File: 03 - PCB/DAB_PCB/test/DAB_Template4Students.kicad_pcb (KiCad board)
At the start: 2 copper layers, 240 x 200 mm, 32 parts

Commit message: lined almost every footprint
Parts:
- added C25: 1000pF, Capacitor_SMD:C_1206_3216Metric, F.Cu at (221.6, 79.1)
- added C5: 1000pF, Capacitor_SMD:C_1206_3216Metric, F.Cu at (221.6, 75.7)
- added C_boot1: 100nF, Capacitor_SMD:C_1206_3216Metric, F.Cu at (129.7, 124.8)
- added C_boot2: 100nF, Capacitor_SMD:C_1206_3216Metric, F.Cu at (129.7, 128.1)
- added C_boot3: 0.22µF, Capacitor_SMD:C_1206_3216Metric, F.Cu at (136.7, 137.2)
- added C_boot4: 0.22µF, Capacitor_SMD:C_1206_3216Metric, F.Cu at (136.7, 140.5)
- added C_fil1: 2.2µF, Capacitor_SMD:C_1206_3216Metric, F.Cu at (221.6, 82.4)
- added C_fil2: 2.2µF, Capacitor_SMD:C_1206_3216Metric, F.Cu at (221.6, 85.8)
- added C_fil3: 2.2µF, Capacitor_SMD:C_1206_3216Metric, F.Cu at (221.6, 89.1)
- added C_vdd1: 2.2µF, Capacitor_SMD:C_1206_3216Metric, F.Cu at (129.7, 131.5)
- added C_vdd2: 2.2µF, Capacitor_SMD:C_1206_3216Metric, F.Cu at (129.7, 134.8)
- added C_vdd3: 4.7µF, Capacitor_SMD:C_1206_3216Metric, F.Cu at (136.7, 143.9)
- added C_vdd4: 4.7µF, Capacitor_SMD:C_1206_3216Metric, F.Cu at (136.7, 147.2)
- added C_vdd5: 10nF, Capacitor_SMD:C_1206_3216Metric, F.Cu at (221.6, 92.5)
- added C_vdd6: 10nF, Capacitor_SMD:C_1206_3216Metric, F.Cu at (221.6, 95.8)
- added Chi1: 22pF, Capacitor_SMD:C_1206_3216Metric, F.Cu at (142.4, 137.2)
- added Chi2: 22pF, Capacitor_SMD:C_1206_3216Metric, F.Cu at (142.4, 140.5)
- added Chi3: 22pF, Capacitor_SMD:C_1206_3216Metric, F.Cu at (142.4, 143.9)
- added Chi4: 22pF, Capacitor_SMD:C_1206_3216Metric, F.Cu at (142.4, 147.2)
- added Cli1: 22pF, Capacitor_SMD:C_1206_3216Metric, F.Cu at (148.0, 137.2)
- added Cli2: 22pF, Capacitor_SMD:C_1206_3216Metric, F.Cu at (148.0, 140.5)
- added Cli3: 22pF, Capacitor_SMD:C_1206_3216Metric, F.Cu at (148.0, 143.9)
- added Cli4: 22pF, Capacitor_SMD:C_1206_3216Metric, F.Cu at (148.0, 147.2)
- added D1: LMB14S-TP, DAB:LMB14STP, F.Cu at (197.9, 163.0)
- added IC1: UCC27288DR, DAB:SOIC127P600X175-8N, F.Cu at (122.7, 119.8)
- added IC2: UCC27288DR, DAB:SOIC127P600X175-8N, F.Cu at (122.6, 126.4)
- added IC3: UCC27288DR, DAB:SOIC127P600X175-8N, F.Cu at (122.6, 132.9)
- added IC4: UCC27288DR, DAB:SOIC127P600X175-8N, F.Cu at (122.6, 139.5)
- added IC5: INA201AID, DAB:SOIC127P600X175-8N, F.Cu at (206.3, 77.3)
- added IC6: INA201AID, DAB:SOIC127P600X175-8N, F.Cu at (206.3, 83.9)
- added IC7: INA201AID, DAB:SOIC127P600X175-8N, F.Cu at (206.3, 90.4)
- added IC8: INA201AID, DAB:SOIC127P600X175-8N, F.Cu at (206.3, 97.0)
- added LED1: WP710A10LGD, DAB:WP710A10LID, F.Cu at (171.8, 160.1)
- added LED2: WP710A10LGD, DAB:WP710A10LID, F.Cu at (178.1, 160.1)
- added LED3: WP710A10LGD, DAB:WP710A10LID, F.Cu at (184.4, 160.1)
- added LED4: WP710A10LGD, DAB:WP710A10LID, F.Cu at (190.7, 160.1)
- added LED4: WP710A10LGD, DAB:WP710A10LID, F.Cu at (227.6, 76.3)
- added LED6: WP710A10LID, DAB:WP710A10LID, F.Cu at (171.8, 167.1)
- added LED7: WP710A10LGD, DAB:WP710A10LID, F.Cu at (178.1, 167.1)
- added LED8: WP710A10LGD, DAB:WP710A10LID, F.Cu at (184.4, 167.1)
- added R17: 200k, Resistor_SMD:R_1206_3216Metric, F.Cu at (204.8, 59.2)
- added R18: 50, Resistor_SMD:R_1206_3216Metric, F.Cu at (204.8, 62.5)
- added R19: 50, Resistor_SMD:R_1206_3216Metric, F.Cu at (204.8, 65.8)
- added Rdiv1: 23.2k, Resistor_SMD:R_1206_3216Metric, F.Cu at (204.8, 69.1)
- added Rdiv2: 10k, Resistor_SMD:R_1206_3216Metric, F.Cu at (204.8, 72.4)
- added Rdiv3: 23.2k, Resistor_SMD:R_1206_3216Metric, F.Cu at (210.4, 59.2)
- added Rdiv4: 10k, Resistor_SMD:R_1206_3216Metric, F.Cu at (210.4, 62.5)
- added Rfil1: 10, Resistor_SMD:R_1206_3216Metric, F.Cu at (210.4, 65.8)
- added Rfil2: 10, Resistor_SMD:R_1206_3216Metric, F.Cu at (210.4, 69.1)
- added Rfil5: 10, Resistor_SMD:R_1206_3216Metric, F.Cu at (210.4, 72.4)
- added Rfil6: 10, Resistor_SMD:R_1206_3216Metric, F.Cu at (216.0, 59.2)
- added Rfil8: 10, Resistor_SMD:R_1206_3216Metric, F.Cu at (216.0, 62.5)
- added Rfil9: 10, Resistor_SMD:R_1206_3216Metric, F.Cu at (216.0, 65.8)
- added Rg1: 10, Resistor_SMD:R_1206_3216Metric, F.Cu at (136.7, 117.3)
- added Rg2: 10, Resistor_SMD:R_1206_3216Metric, F.Cu at (136.7, 120.6)
- added Rg3: 10, Resistor_SMD:R_1206_3216Metric, F.Cu at (136.7, 123.9)
- added Rg4: 10, Resistor_SMD:R_1206_3216Metric, F.Cu at (136.7, 127.2)
- added Rg5: 10, Resistor_SMD:R_1206_3216Metric, F.Cu at (136.7, 130.5)
- added Rg6: 10, Resistor_SMD:R_1206_3216Metric, F.Cu at (136.7, 133.8)
- added Rg7: 10, Resistor_SMD:R_1206_3216Metric, F.Cu at (142.3, 117.3)
- added Rg8: 10, Resistor_SMD:R_1206_3216Metric, F.Cu at (142.3, 120.6)
- added Rgs1: 10k, Resistor_SMD:R_1206_3216Metric, F.Cu at (142.3, 123.9)
- added Rgs2: 10k, Resistor_SMD:R_1206_3216Metric, F.Cu at (142.3, 127.2)
- added Rgs3: 10k, Resistor_SMD:R_1206_3216Metric, F.Cu at (142.3, 130.5)
- added Rgs4: 10k, Resistor_SMD:R_1206_3216Metric, F.Cu at (142.3, 133.8)
- added Rgs5: 10k, Resistor_SMD:R_1206_3216Metric, F.Cu at (147.9, 117.3)
- added Rgs6: 10k, Resistor_SMD:R_1206_3216Metric, F.Cu at (147.9, 120.6)
- added Rgs7: 10k, Resistor_SMD:R_1206_3216Metric, F.Cu at (147.9, 123.9)
- added Rgs8: 10k, Resistor_SMD:R_1206_3216Metric, F.Cu at (147.9, 127.2)
- added Rhi1: 2.2k, Resistor_SMD:R_1206_3216Metric, F.Cu at (147.9, 130.5)
- added Rhi2: 2.2k, Resistor_SMD:R_1206_3216Metric, F.Cu at (147.9, 133.8)
- added Rhi3: 2.2k, Resistor_SMD:R_1206_3216Metric, F.Cu at (153.5, 117.3)
- added Rhi4: 2.2k, Resistor_SMD:R_1206_3216Metric, F.Cu at (153.5, 120.6)
- added Rli1: 2.2k, Resistor_SMD:R_1206_3216Metric, F.Cu at (153.5, 123.9)
- added Rli2: 2.2k, Resistor_SMD:R_1206_3216Metric, F.Cu at (153.5, 127.2)
- added Rli3: 2.2k, Resistor_SMD:R_1206_3216Metric, F.Cu at (153.5, 130.5)
- added Rli4: 2.2k, Resistor_SMD:R_1206_3216Metric, F.Cu at (153.5, 133.8)
- added RrtE1: Variable Resistor, DAB:TRIMMER CT-6EP, F.Cu at (214.6, 78.2)
- added RrtE2: 10k, DAB:TRIMMER CT-6EP, F.Cu at (214.6, 86.4)
- added RrtE3: 10k, DAB:TRIMMER CT-6EP, F.Cu at (214.6, 94.7)
- added Shunt1: 25m, Resistor_SMD:R_2512_6332Metric, F.Cu at (223.2, 60.0)
- added Shunt2: 10m, Resistor_SMD:R_2512_6332Metric, F.Cu at (223.2, 64.9)
- added Shunt3: 10m, Resistor_SMD:R_2512_6332Metric, F.Cu at (223.2, 69.8)
- added Tr1: Transformer, DAB:B66362X1014T001, F.Cu at (207.2, 122.1)
- moved C? 220.5 mm to (119.5, 33.0)
- moved D? 220.5 mm to (110.0, 95.0)
- moved J? 220.5 mm to (69.6, 70.5)
- moved LED? 220.5 mm to (158.6, 31.9)
- moved Me? 220.5 mm to (59.8, 32.0)
- moved Me? 220.5 mm to (65.8, 32.0)
- moved R? 220.5 mm to (62.3, 94.2)
- moved R? 220.5 mm to (99.8, 33.0)
- moved SWH?? 220.5 mm to (145.8, 35.6)
- moved C? 220.5 mm to (110.8, 33.0)
- moved C? 220.5 mm to (115.2, 33.0)
- moved D? 220.5 mm to (148.8, 96.0)
- moved HS? 220.5 mm to (129.0, 78.5)
- moved IC? 220.5 mm to (85.6, 95.0)
- moved IC? 220.5 mm to (102.7, 94.1)
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
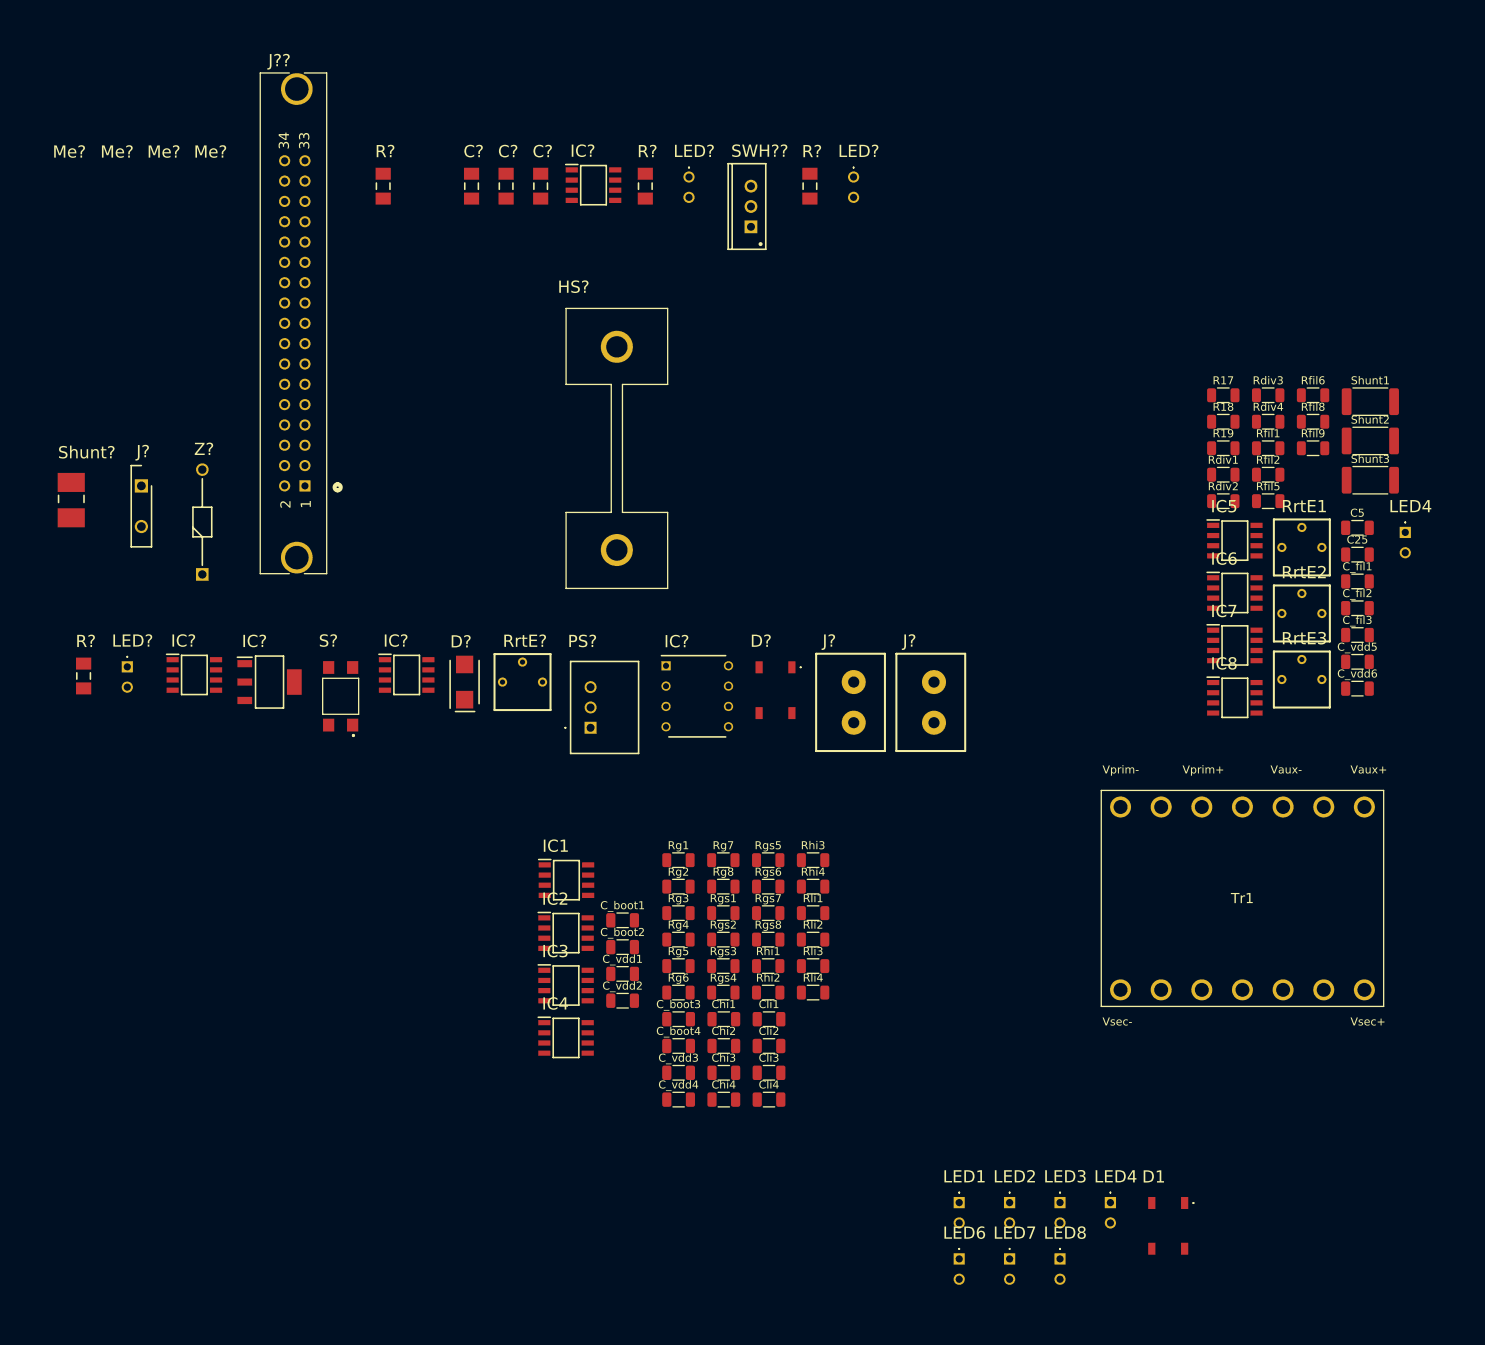
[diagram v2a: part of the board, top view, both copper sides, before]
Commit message: added testpoints
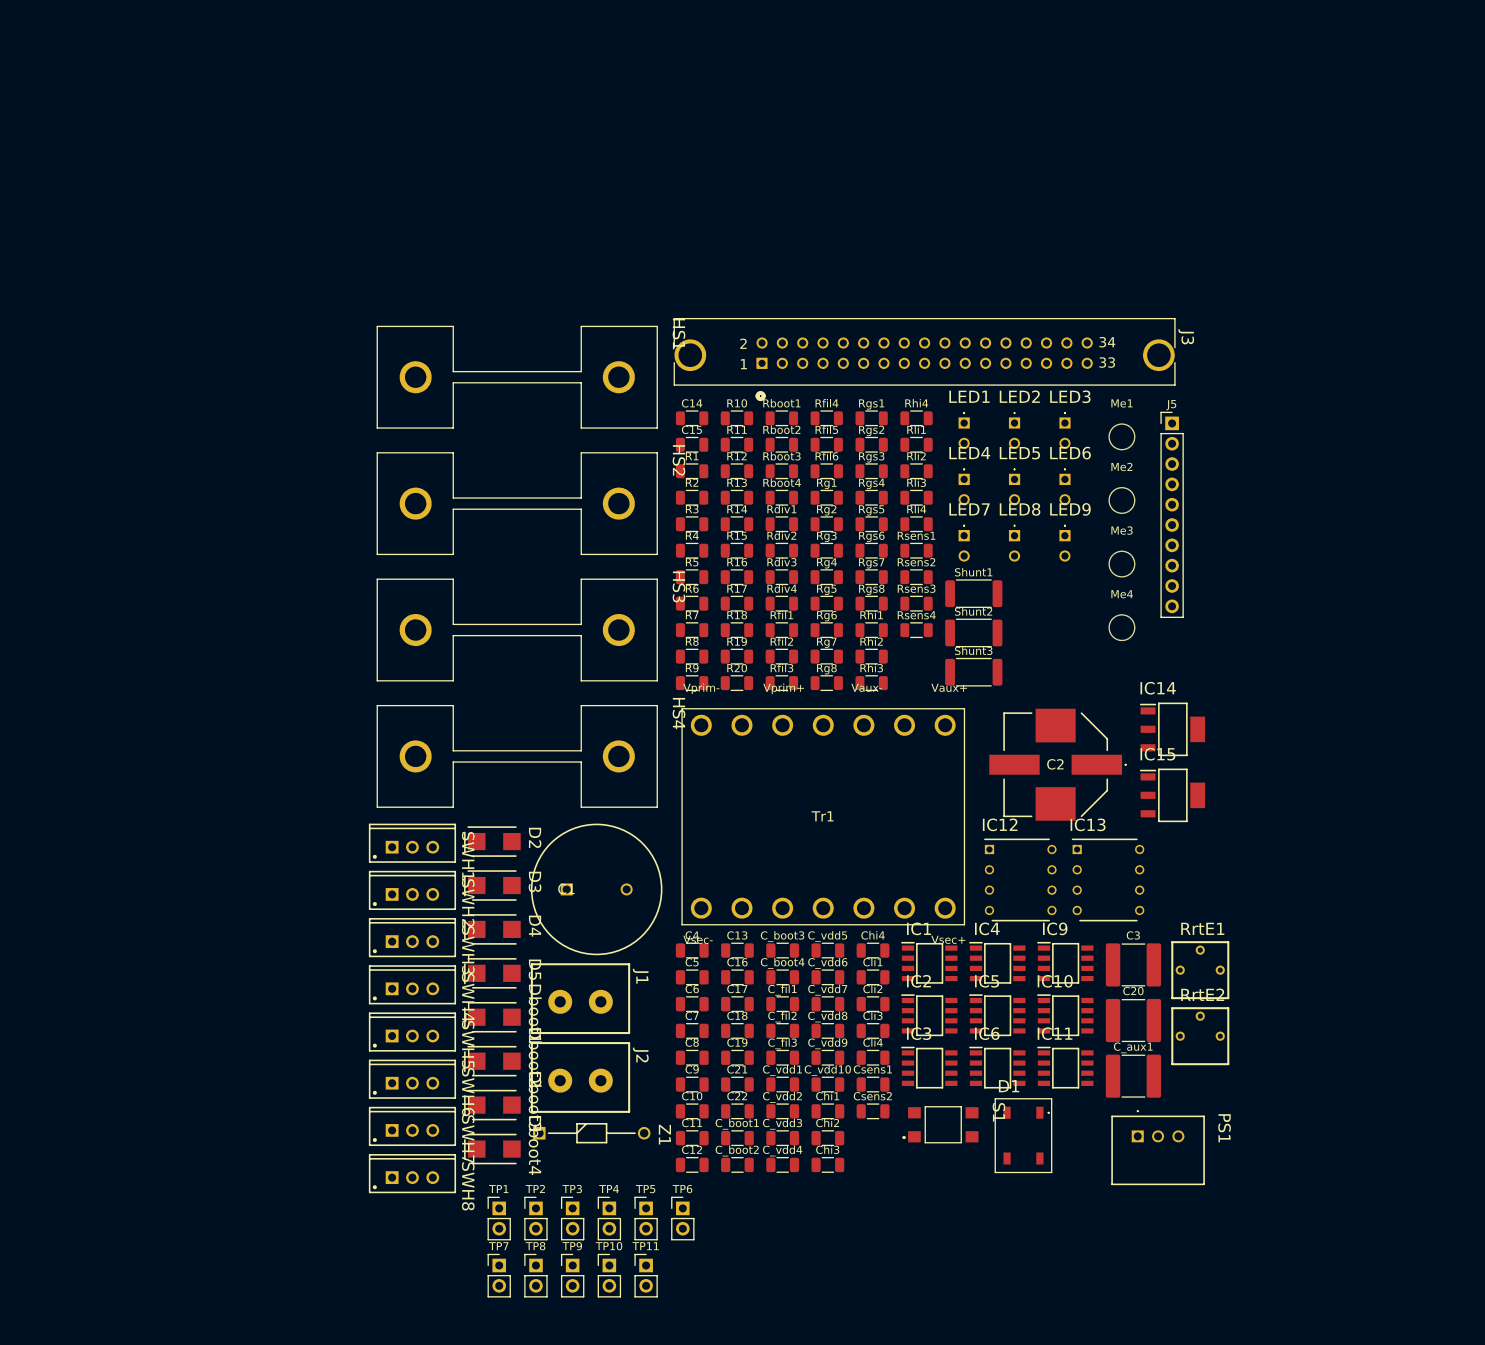
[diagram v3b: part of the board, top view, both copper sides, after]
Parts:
- removed C25: 1000pF, Capacitor_SMD:C_1206_3216Metric
- removed C? (x2): 1uF, DAB_EE365:1206
- removed C?: Put Value Here!, DAB_EE365:1206
- removed D?: LMB14S-TP, DAB_EE365:LMB14STP
- removed D?: ES2C, DAB_EE365:DIOM5436X244N
- removed HS?: Heatsink, DAB_EE365:Heatsink EA-T220
- removed IC7, IC8: INA201AID, DAB:SOIC127P600X175-8N
- removed IC?: AZ1117IH-3.3TRG1, DAB_EE365:SOT230P700X180-4N
- removed IC?: INA201AID, DAB_EE365:SOIC127P600X175-8N
- removed IC?: MCP6241-E_P, DAB_EE365:DIP781W56P254L950H533Q8N
- removed IC?: UCC27288DR, DAB_EE365:SOIC127P600X175-8N
- removed IC?: UA78L12ACDR, DAB_EE365:SOIC127P600X175-8N
- removed J?: test point, DAB_EE365:test point
- removed J? (x2): , DAB_EE365:PHOENIX 1755736
- removed J??: N3431-6302RB, DAB_EE365:3M_N3431-6302RB
- removed the LED4 at (190.7, 160.1)
- removed the LED4 at (227.6, 76.3)
- removed LED? (x2): WP710A10LGD, DAB_EE365:WP710A10LGD
- removed LED?: WP710A10LID, DAB_EE365:WP710A10LID
- removed Me? (x4): M3-Hole, DAB_EE365:M3
- removed PS?: 173951275, DAB_EE365:173951275
- removed R? (x4): Put Value here!, DAB_EE365:1206
- removed Rfil8, Rfil9: 10, Resistor_SMD:R_1206_3216Metric
- removed RrtE3: 10k, DAB:TRIMMER CT-6EP
- removed RrtE?: Variable Resistor, DAB_EE365:TRIMMER CT-6EP
- removed S?: TL3305BF100QG, DAB_EE365:TL3305BF160QG
- removed SWH??: Put MOSFET Part Number Here!, PCB1:TO-220AB
- removed Shunt?: Put Value Here!, DAB_PCB:CSNL2512FT5L00
- removed Z?: 1N4750A-TR, SamacSys:DIOAD1310W86L370D235
- added C1: 680µF, DAB:CAPPRD750W80D1625H3750, F.Cu at (122.7, 120.9)
- added C10: 10µF, Capacitor_SMD:C_1206_3216Metric, F.Cu at (138.4, 148.7)
- added C11: 10µF, Capacitor_SMD:C_1206_3216Metric, F.Cu at (138.4, 152.0)
- added C12: 10µF, Capacitor_SMD:C_1206_3216Metric, F.Cu at (138.4, 155.4)
- added C13: 10µF, Capacitor_SMD:C_1206_3216Metric, F.Cu at (144.1, 128.6)
- added C14: 1uF, Resistor_SMD:R_1206_3216Metric, F.Cu at (138.4, 62.0)
- added C15: 1uF, Resistor_SMD:R_1206_3216Metric, F.Cu at (138.4, 65.3)
- added C16: 1000pF, Capacitor_SMD:C_1206_3216Metric, F.Cu at (144.1, 131.9)
- added C17: 1000pF, Capacitor_SMD:C_1206_3216Metric, F.Cu at (144.1, 135.3)
- added C18: 1000pF, Capacitor_SMD:C_1206_3216Metric, F.Cu at (144.1, 138.6)
- added C19: 1000pF, Capacitor_SMD:C_1206_3216Metric, F.Cu at (144.1, 142.0)
- added C2: 1000µF, DAB:MAL215097614E3, F.Cu at (183.9, 105.3)
- added C20: 22µF, Capacitor_SMD:C_2220_5750Metric, F.Cu at (193.6, 137.3)
- added C21: 4.7µF, Capacitor_SMD:C_1206_3216Metric, F.Cu at (144.1, 145.3)
- added C22: 4.7µF, Capacitor_SMD:C_1206_3216Metric, F.Cu at (144.1, 148.7)
- added C3: 22µF, Capacitor_SMD:C_2220_5750Metric, F.Cu at (193.6, 130.4)
- added C4: 10µF, Capacitor_SMD:C_1206_3216Metric, F.Cu at (138.4, 128.6)
- added C6: 100nF, Capacitor_SMD:C_1206_3216Metric, F.Cu at (138.4, 135.3)
- added C7: 330nF, Capacitor_SMD:C_1206_3216Metric, F.Cu at (138.4, 138.6)
- added C8: 10µF, Capacitor_SMD:C_1206_3216Metric, F.Cu at (138.4, 142.0)
- added C9: 10µF, Capacitor_SMD:C_1206_3216Metric, F.Cu at (138.4, 145.3)
- added C_aux1: 22nF, Capacitor_SMD:C_2220_5750Metric, F.Cu at (193.6, 144.3)
- added C_vdd10: 10nF, Capacitor_SMD:C_1206_3216Metric, F.Cu at (155.4, 145.3)
- added C_vdd7: 1µF, Capacitor_SMD:C_1206_3216Metric, F.Cu at (155.4, 135.3)
- added C_vdd8: 1µF, Capacitor_SMD:C_1206_3216Metric, F.Cu at (155.4, 138.6)
- added C_vdd9: 10nF, Capacitor_SMD:C_1206_3216Metric, F.Cu at (155.4, 142.0)
- added Csens1: 4.7nF, Capacitor_SMD:C_1206_3216Metric, F.Cu at (161.0, 145.3)
- added Csens2: 2.2nF, Capacitor_SMD:C_1206_3216Metric, F.Cu at (161.0, 148.7)
- added D2: ES2C, DAB:DIOM5436X244N, F.Cu at (113.7, 114.9)
- added D3: ES2C, DAB:DIOM5436X244N, F.Cu at (113.7, 120.4)
- added D4: ES2C, DAB:DIOM5436X244N, F.Cu at (113.7, 125.9)
- added D5: ES2C, DAB:DIOM5436X244N, F.Cu at (113.7, 131.4)
- added Dboot1: ES2C, DAB:DIOM5436X244N, F.Cu at (113.7, 136.9)
- added Dboot2: ES2C, DAB:DIOM5436X244N, F.Cu at (113.7, 142.4)
- added Dboot3: ES2C, DAB:DIOM5436X244N, F.Cu at (113.7, 147.9)
- added Dboot4: ES2C, DAB:DIOM5436X244N, F.Cu at (113.7, 153.4)
- added HS1: Heatsink, DAB:Heatsink EA-T220, F.Cu at (103.9, 56.9)
- added HS2: Heatsink, DAB:Heatsink EA-T220, F.Cu at (103.9, 72.7)
- added HS3: Heatsink, DAB:Heatsink EA-T220, F.Cu at (103.9, 88.5)
- added HS4: Heatsink, DAB:Heatsink EA-T220, F.Cu at (103.9, 104.3)
- added IC10: INA201AID, DAB:SOIC127P600X175-8N, F.Cu at (185.1, 136.7)
- added IC11: INA201AID, DAB:SOIC127P600X175-8N, F.Cu at (185.1, 143.3)
- added IC12: MCP6241-E_P, DAB:DIP781W56P254L950H533Q8N, F.Cu at (179.5, 119.7)
- added IC13: MCP6241-E_P, DAB:DIP781W56P254L950H533Q8N, F.Cu at (190.4, 119.7)
- added IC14: ~, DAB:SOT230P700X180-4N, F.Cu at (198.5, 100.9)
- added IC15: ~, DAB:SOT230P700X180-4N, F.Cu at (198.5, 109.2)
- added IC9: INA201AID, DAB:SOIC127P600X175-8N, F.Cu at (185.1, 130.2)
- added J1: ~, DAB:PHOENIX 1755736, F.Cu at (127.0, 135.0)
- added J2: ~, DAB:PHOENIX 1755736, F.Cu at (127.0, 144.8)
- added J3: N3431-6302RB, DAB:3M_N3431-6302RB, F.Cu at (187.8, 52.6)
- added J5: Conn_01x10_Pin, Connector_PinHeader_2.54mm:PinHeader_1x10_P2.54mm_Vertical, F.Cu at (198.4, 62.7)
- added LED4: WP710A10LGD, DAB:WP710A10LID, F.Cu at (172.4, 69.7)
- added LED5: WP710A10LGD, DAB:WP710A10LID, F.Cu at (178.7, 69.7)
- added LED9: WP710A10LGD, DAB:WP710A10LID, F.Cu at (185.0, 76.7)
- added Me1: M3-Hole, MountingHole:MountingHole_3.2mm_M3, F.Cu at (192.1, 64.4)
- added Me2: M3-Hole, MountingHole:MountingHole_3.2mm_M3, F.Cu at (192.1, 72.3)
- added Me3: M3-Hole, MountingHole:MountingHole_3.2mm_M3, F.Cu at (192.1, 80.3)
- added Me4: M3-Hole, MountingHole:MountingHole_3.2mm_M3, F.Cu at (192.1, 88.2)
- added PS1: 173951275, DAB:173951275, F.Cu at (194.1, 151.8)
- added R1: 27.4k, Resistor_SMD:R_1206_3216Metric, F.Cu at (138.4, 68.7)
- added R10: 680, Resistor_SMD:R_1206_3216Metric, F.Cu at (144.0, 62.0)
- added R11: 2.2k, Resistor_SMD:R_1206_3216Metric, F.Cu at (144.0, 65.3)
- added R12: 200k, Resistor_SMD:R_1206_3216Metric, F.Cu at (144.0, 68.7)
- added R13: 680, Resistor_SMD:R_1206_3216Metric, F.Cu at (144.0, 72.0)
- added R14: 10k, Resistor_SMD:R_1206_3216Metric, F.Cu at (144.0, 75.3)
- added R15: 50, Resistor_SMD:R_1206_3216Metric, F.Cu at (144.0, 78.6)
- added R16: 50, Resistor_SMD:R_1206_3216Metric, F.Cu at (144.0, 81.9)
- added R2: 680, Resistor_SMD:R_1206_3216Metric, F.Cu at (138.4, 72.0)
- added R20: 50, Resistor_SMD:R_1206_3216Metric, F.Cu at (144.0, 95.1)
- added R3: 680, Resistor_SMD:R_1206_3216Metric, F.Cu at (138.4, 75.3)
- added R4: 2.2k, Resistor_SMD:R_1206_3216Metric, F.Cu at (138.4, 78.6)
- added R5: 4.99k, Resistor_SMD:R_1206_3216Metric, F.Cu at (138.4, 81.9)
- added R6: 4.99k, Resistor_SMD:R_1206_3216Metric, F.Cu at (138.4, 85.2)
- added R7: 680, Resistor_SMD:R_1206_3216Metric, F.Cu at (138.4, 88.5)
- added R8: 680, Resistor_SMD:R_1206_3216Metric, F.Cu at (138.4, 91.8)
- added R9: 680, Resistor_SMD:R_1206_3216Metric, F.Cu at (138.4, 95.1)
- added Rboot1: 10, Resistor_SMD:R_1206_3216Metric, F.Cu at (149.6, 62.0)
- added Rboot2: 10, Resistor_SMD:R_1206_3216Metric, F.Cu at (149.6, 65.3)
- added Rboot3: 4.99, Resistor_SMD:R_1206_3216Metric, F.Cu at (149.6, 68.7)
- added Rboot4: 4.99, Resistor_SMD:R_1206_3216Metric, F.Cu at (149.6, 72.0)
- added Rfil3: 10, Resistor_SMD:R_1206_3216Metric, F.Cu at (149.6, 95.1)
- added Rfil4: 10, Resistor_SMD:R_1206_3216Metric, F.Cu at (155.2, 62.0)
- added Rsens1: 97.6k, Resistor_SMD:R_1206_3216Metric, F.Cu at (166.5, 78.6)
- added Rsens2: 39.2k, Resistor_SMD:R_1206_3216Metric, F.Cu at (166.5, 81.9)
- added Rsens3: 4.32k, Resistor_SMD:R_1206_3216Metric, F.Cu at (166.5, 85.2)
- added Rsens4: 10k, Resistor_SMD:R_1206_3216Metric, F.Cu at (166.5, 88.5)
- added S1: TL3305BF100QG, DAB:TL3305BF160QG, F.Cu at (169.8, 150.3)
- added SWH1: PHP18NQ11T, DAB:TO-220AB, F.Cu at (103.5, 115.7)
- added SWH2: PHP18NQ11T, DAB:TO-220AB, F.Cu at (103.5, 121.6)
- added SWH3: IRLB8743PbF, DAB:TO-220AB, F.Cu at (103.5, 127.5)
- added SWH4: IRLB8743PbF, DAB:TO-220AB, F.Cu at (103.5, 133.4)
- added SWH5: PHP18NQ11T, DAB:TO-220AB, F.Cu at (103.5, 139.3)
- added SWH6: IRLB8743PbF, DAB:TO-220AB, F.Cu at (103.5, 145.2)
- added SWH7: PHP18NQ11T, DAB:TO-220AB, F.Cu at (103.5, 151.1)
- added SWH8: IRLB8743PbF, DAB:TO-220AB, F.Cu at (103.5, 157.0)
- added TP1: Vds1, Connector_PinHeader_2.54mm:PinHeader_1x02_P2.54mm_Vertical, F.Cu at (114.3, 160.8)
- added TP10: sec, Connector_PinHeader_2.54mm:PinHeader_1x02_P2.54mm_Vertical, F.Cu at (128.1, 167.9)
- added TP11: ac, Connector_PinHeader_2.54mm:PinHeader_1x02_P2.54mm_Vertical, F.Cu at (132.7, 167.9)
- added TP2: Vds3, Connector_PinHeader_2.54mm:PinHeader_1x02_P2.54mm_Vertical, F.Cu at (118.9, 160.8)
- added TP3: Vds5, Connector_PinHeader_2.54mm:PinHeader_1x02_P2.54mm_Vertical, F.Cu at (123.5, 160.8)
- added TP4: Vds7, Connector_PinHeader_2.54mm:PinHeader_1x02_P2.54mm_Vertical, F.Cu at (128.1, 160.8)
- added TP5: Vgs2, Connector_PinHeader_2.54mm:PinHeader_1x02_P2.54mm_Vertical, F.Cu at (132.7, 160.8)
- added TP6: Vgs4, Connector_PinHeader_2.54mm:PinHeader_1x02_P2.54mm_Vertical, F.Cu at (137.2, 160.8)
- added TP7: Vgs6, Connector_PinHeader_2.54mm:PinHeader_1x02_P2.54mm_Vertical, F.Cu at (114.3, 167.9)
- added TP8: Vgs8, Connector_PinHeader_2.54mm:PinHeader_1x02_P2.54mm_Vertical, F.Cu at (118.9, 167.9)
- added TP9: prim, Connector_PinHeader_2.54mm:PinHeader_1x02_P2.54mm_Vertical, F.Cu at (123.5, 167.9)
- added Z1: 1N4750A-TR, DAB:DIOAD1310W86L370D235, F.Cu at (119.3, 151.4)
- C5: value 1000pF -> 0.1µF
- IC5: value INA201AID -> UA78L12ACDR
- LED1: value WP710A10LGD -> WP710A10LID
- LED6: value WP710A10LID -> WP710A10LGD
- R17: value 200k -> 10k
- R18: value 50 -> 10k
- RrtE1: value Variable Resistor -> 10k
- moved C5 100.4 mm to (138.4, 131.9)
- moved LED6 98.3 mm to (185.0, 69.7)
- moved LED1 97.4 mm to (172.4, 62.6)
- moved LED2 97.4 mm to (178.7, 62.6)
- moved LED3 97.4 mm to (185.0, 62.6)
- moved LED7 90.6 mm to (172.4, 76.7)
- moved LED8 90.6 mm to (178.7, 76.7)
- moved C_fil3 89.2 mm to (149.7, 142.0)
- moved C_fil1 89.2 mm to (149.7, 135.3)
- moved C_fil2 89.2 mm to (149.7, 138.6)
- moved C_vdd5 75.4 mm to (155.4, 128.6)
- moved C_vdd6 75.4 mm to (155.4, 131.9)
- moved IC5 66.4 mm to (176.6, 136.7)
- moved IC6 66.4 mm to (176.6, 143.3)
- moved R17 66.1 mm to (144.0, 85.2)
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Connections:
- C5 pad 2: /ADCA0 -> 12Vsec
- C_boot1 pad 1: /vs1 -> /ac-
- C_boot1 pad 2: Net-(Dboot1-K) -> Net-(Dboot2-K)
- C_boot2 pad 1: /ac- -> /vs1
- C_boot2 pad 2: Net-(Dboot2-K) -> Net-(Dboot1-K)
- C_boot3 pad 1: /vs5 -> /vs7
- C_boot4 pad 1: /vs7 -> /vs5
- C_fil1 pad 1: Net-(IC5-V_IN-) -> Net-(IC6-V_IN-)
- C_fil1 pad 2: Net-(IC5-V_IN+) -> Net-(IC6-V_IN+)
- C_fil2 pad 1: Net-(IC6-V_IN-) -> Net-(IC10-V_IN-)
- C_fil2 pad 2: Net-(IC6-V_IN+) -> Net-(IC10-V_IN+)
- C_fil3 pad 1: Net-(IC7-V_IN-) -> Net-(IC11-V_IN-)
- C_vdd1 pad 2: 12Vpri -> 12Vsec
- C_vdd2 pad 2: 12Vpri -> 12Vsec
- Chi1 pad 2: Net-(IC2-HI) -> Net-(IC1-HI)
- Chi2 pad 2: Net-(IC1-HI) -> Net-(IC2-HI)
- D1 pad 1: /aux -> aux
- IC1 pad 1: 12Vpri -> 12Vsec
- IC2 pad 1: 12Vpri -> 12Vsec
- IC3 pad 4: /vs5 -> /vs7
- IC4 pad 4: /vs7 -> /vs5
- IC5 pad 1: 3V3pri -> 12Vsec
- IC5 pad 2: Net-(IC5-OUT) -> GND
- IC5 pad 3: unconnected-(IC5-CMP_IN-Pad3) -> GND
- IC5 pad 4: GND -> unconnected-(IC5-NC_1-Pad4)
- IC5 pad 6: unconnected-(IC5-CMP_OUT-Pad6) -> GND
- IC5 pad 7: Net-(IC5-V_IN-) -> GND
- IC5 pad 8: Net-(IC5-V_IN+) -> aux
- IC6 pad 1: 3V3sec -> 3V3pri
- IC6 pad 3: unconnected-(IC6-CMP_IN-Pad3) -> Net-(IC6-CMP_IN)
- IC6 pad 5: unconnected-(IC6-~{RESET}-Pad5) -> 3V3pri
- IC6 pad 6: unconnected-(IC6-CMP_OUT-Pad6) -> Net-(D2-A)
- LED1 pad 1: Net-(LED1-K) -> GND
- LED1 pad 2: 3V3pri -> Net-(LED1-A)
- LED2 pad 2: 12Vpri -> 12Vsec
- LED3 pad 2: Net-(LED3-A) -> 12Vsec
- LED7 pad 1: GND -> Net-(LED7-K)
- LED7 pad 2: Net-(LED7-A) -> 3V3pri
- LED8 pad 1: GND -> Net-(LED8-K)
- LED8 pad 2: Net-(LED8-A) -> 3V3sec
- R17 pad 1: GND -> Net-(IC12-VIN-)
- R17 pad 2: Net-(D2-K) -> Net-(IC12-VOUT)
- R18 pad 1: /ADCA0 -> Net-(IC13-VIN-)
- R18 pad 2: Net-(IC5-OUT) -> Net-(IC13-VOUT)
- R19 pad 1: /ADCB0 -> Net-(IC12-VOUT)
- R19 pad 2: Net-(IC6-OUT) -> /ADCA1
- Rdiv1 pad 1: Net-(IC7-CMP_IN) -> Net-(IC6-CMP_IN)
- Rdiv2 pad 2: Net-(IC7-CMP_IN) -> Net-(IC6-CMP_IN)
- Rfil1 pad 1: Net-(IC5-V_IN+) -> Net-(IC6-V_IN+)
- Rfil1 pad 2: /prim+ -> /ac+
- Rfil2 pad 1: Net-(IC5-V_IN-) -> Net-(IC6-V_IN-)
- Rfil2 pad 2: /prim- -> /ac-
- Rfil5 pad 1: Net-(IC6-V_IN+) -> Net-(IC10-V_IN-)
- Rfil5 pad 2: /sec+ -> /prim-
- Rfil6 pad 1: Net-(IC6-V_IN-) -> Net-(IC11-V_IN-)
- Rg1 pad 1: Net-(IC1-HO) -> /vg2
- Rg1 pad 2: /vg1 -> Net-(IC1-LO)
- Rg2 pad 1: /vg2 -> /vg4
- Rg2 pad 2: Net-(IC1-LO) -> Net-(IC2-LO)
- Rg3 pad 1: Net-(IC2-HO) -> /vg8
- Rg3 pad 2: /vg3 -> Net-(IC3-LO)
- Rg4 pad 1: /vg4 -> /vg6
- Rg4 pad 2: Net-(IC2-LO) -> Net-(IC4-LO)
- Rg5 pad 1: Net-(IC3-HO) -> Net-(IC1-HO)
- Rg5 pad 2: /vg5 -> /vg1
- Rg6 pad 1: /vg6 -> Net-(IC2-HO)
- Rg6 pad 2: Net-(IC3-LO) -> /vg3
- Rg7 pad 1: Net-(IC4-HO) -> Net-(IC3-HO)
- Rg8 pad 1: /vg8 -> Net-(IC4-HO)
- Rg8 pad 2: Net-(IC4-LO) -> /vg5
- Rgs1 pad 1: /vs1 -> GND
- Rgs1 pad 2: /vg1 -> /vg2
- Rgs2 pad 2: /vg2 -> /vg4
- Rgs3 pad 1: /ac- -> GND
- Rgs3 pad 2: /vg3 -> /vg8
- Rgs4 pad 2: /vg4 -> /vg6
- Rgs5 pad 1: /vs5 -> /vs1
- Rgs5 pad 2: /vg5 -> /vg1
- Rgs6 pad 1: GND -> /ac-
- Rgs6 pad 2: /vg6 -> /vg3
- Rgs8 pad 1: GND -> /vs5
- Rgs8 pad 2: /vg8 -> /vg5
- Rhi1 pad 1: Net-(IC2-HI) -> Net-(IC1-HI)
- Rhi1 pad 2: /PWM2B_ISO -> /PWM1B_ISO
- Rhi2 pad 1: Net-(IC1-HI) -> Net-(IC2-HI)
- Rhi2 pad 2: /PWM1B_ISO -> /PWM2B_ISO
- Rhi3 pad 2: /PWM3B_ISO -> /PWM4B_ISO
- Rhi4 pad 2: /PWM4B_ISO -> /PWM3B_ISO
- Rli3 pad 2: /PWM3A_ISO -> /PWM4A_ISO
- Rli4 pad 2: /PWM4A_ISO -> /PWM3A_ISO
- RrtE1 pad 1: unconnected-(RrtE1-Pad1) -> Net-(IC6-OUT)
- RrtE1 pad 2: unconnected-(RrtE1-Pad2) -> Net-(Rdiv1-Pad2)
- RrtE2 pad 2: Net-(Rdiv1-Pad2) -> Net-(Rdiv3-Pad2)
- Shunt2 pad 1: /ac- -> /sec+
- Shunt2 pad 2: /ac+ -> /sec-
- Shunt3 pad 1: /sec+ -> /ac-
- Shunt3 pad 2: /sec- -> /ac+
